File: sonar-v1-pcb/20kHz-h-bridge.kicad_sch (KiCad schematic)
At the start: 1 part, among them U34 DRV8876PWPR

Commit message: Do some power work
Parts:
- added C6: 22nF, GS_Capacitors:C_0603_1608Metric, symbol GS_Capacitor_0603:C_0603_22nF
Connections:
- net at U34.13 (CPH): now also C6.1
- net at U34.14 (CPL): now also C6.2
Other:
- moved on the sheet: U34
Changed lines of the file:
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@@
 		(comment 1 "George Sleen")
+	)
+	(wire
+		(pts
+			(xy 180.34 86.36) (xy 167.64 86.36)
+		)
+		(stroke
+			(width 0)
+			(type default)
+		)
+	)
+	(wire
+		(pts
+			(xy 180.34 78.74) (xy 167.64 78.74)
+		)
+		(stroke
+			(width 0)
+			(type default)
+		)
 	)
 	(symbol
 		(lib_id "GS_H_Bridges:DRV8876PWPR")
-		(at 148.59 104.14 0)
+		(at 147.32 102.87 0)
 		(unit 1)
 		(body_style 1)
@@
 		(fields_autoplaced yes)
 		(property "Reference" "U34"
-			(at 148.59 69.85 0)
+			(at 147.32 68.58 0)
 			(show_name no)
 			(do_not_autoplace no)
@@
 		)
 		(property "Value" "DRV8876PWPR"
-			(at 148.59 72.39 0)
+			(at 147.32 71.12 0)
 			(show_name no)
 			(do_not_autoplace no)
@@
 		)
 		(property "Footprint" "GS_SO:HTSSOP-16-1EP_4.4x5mm_P0.65mm_EP3.4x5mm_Mask2.46x2.31mm"
-			(at 148.59 53.34 0)
+			(at 147.32 52.07 0)
 			(hide yes)
 			(show_name no)
@@
 		)
 		(property "Datasheet" "https://lcsc.com/product-detail/Motor-Drivers_Texas-Instruments-Texas-Instruments-DRV8876PWPR_C575551.html"
-			(at 148.59 43.18 0)
+			(at 147.32 41.91 0)
 			(hide yes)
 			(show_name no)
@@
 		)
 		(property "Description" "H-Bridge wih Integrated Current Sense and Regulation, 4.5V - 37V Input Voltage Range, 6A Max Current"
-			(at 148.59 45.72 0)
+			(at 147.32 44.45 0)
 			(hide yes)
 			(show_name no)
@@
 		)
 		(property "Manufacturer" "TI"
-			(at 148.59 40.64 0)
+			(at 147.32 39.37 0)
 			(hide yes)
 			(show_name no)
@@
 		)
 		(property "MPN" "DRV8876PWPR"
-			(at 148.59 50.8 0)
+			(at 147.32 49.53 0)
 			(hide yes)
 			(show_name no)
@@
 		)
 		(property "LCSC ID" "C575551"
-			(at 148.59 55.88 0)
+			(at 147.32 54.61 0)
 			(hide yes)
 			(show_name no)
@@
 		)
 		(property "Package" "HTSSOP-16_L5.0-W4.4-P0.65-LS6.4-BL-EP"
-			(at 148.59 48.26 0)
+			(at 147.32 46.99 0)
 			(hide yes)
 			(show_name no)
@@
 					(unit 1)
 				)
+			)
+		)
+	)
+	(symbol
+		(lib_id "GS_Capacitor_0603:C_0603_22nF")
+		(at 180.34 82.55 0)
+		(unit 1)
+		(body_style 1)
+		(exclude_from_sim no)
+		(in_bom yes)
+		(on_board yes)
+		(in_pos_files yes)
+		(dnp no)
+		(fields_autoplaced yes)
+		(property "Reference" "C6"
+			(at 184.15 81.2799 0)
+			(show_name no)
+			(do_not_autoplace no)
+			(effects
+				(font
+					(size 1.27 1.27)
+				)
+				(justify left)
+			)
+		)
+		(property "Value" "22nF"
+			(at 184.15 83.8199 0)
+			(show_name no)
+			(do_not_autoplace no)
+			(effects
+				(font
+					(size 1.27 1.27)
+				)
+				(justify left)
+			)
+		)
+		(property "Footprint" "GS_Capacitors:C_0603_1608Metric"
+			(at 180.34 60.198 0)
+			(hide yes)
+			(show_name no)
+			(do_not_autoplace no)
+			(effects
+				(font
+					(size 1.27 1.27)
+				)
+			)
+		)
+		(property "Datasheet" "https://datasheet.lcsc.com/datasheet/pdf/02336ea48ea44ca18c72517dd3cb7b47.pdf?productCode=C21122"
+			(at 180.34 68.834 0)
+			(hide yes)
+			(show_name no)
+			(do_not_autoplace no)
+			(effects
+				(font
+					(size 1.27 1.27)
+				)
+			)
+		)
+		(property "Description" "22nF 10% Unpolarized Capacitor, 50V Max Voltage, X7R"
+			(at 180.34 66.802 0)
+			(hide yes)
+			(show_name no)
+			(do_not_autoplace no)
+			(effects
+				(font
+					(size 1.27 1.27)
+				)
+			)
+		)
+		(property "Manufacturer" "Samsung Electro-Mechanics"
+			(at 180.34 63.5 0)
+			(hide yes)
+			(show_name no)
+			(do_not_autoplace no)
+			(effects
+				(font
+					(size 1.27 1.27)
+				)
+			)
+		)
+		(property "MPN" "CL10B223KB8NNNC"
+			(at 180.34 65.278 0)
+			(hide yes)
+			(show_name no)
+			(do_not_autoplace no)
+			(effects
+				(font
+					(size 1.27 1.27)
+				)
+			)
+		)
+		(property "LCSC ID" "C21122"
+			(at 180.34 70.612 0)
+			(hide yes)
+			(show_name no)
+			(do_not_autoplace no)
+			(effects
+				(font
+					(size 1.27 1.27)
+				)
+			)
+		)
+		(property "Package" "0603"
+			(at 180.34 61.976 0)
+			(hide yes)
+			(show_name no)
+			(do_not_autoplace no)
+			(effects
+				(font
+					(size 1.27 1.27)
+				)
+			)
+		)
+		(pin "2"
+		)
+		(pin "1"
+		)
+		(instances
+			(project "sonar"
+				(path "/f72ceae0-eee4-4385-b0e8-639846bcb5f2/c6a046af-5387-4c6b-a77e-149ae78eccdc"
+					(reference "C6")
+					(unit 1)
+				)

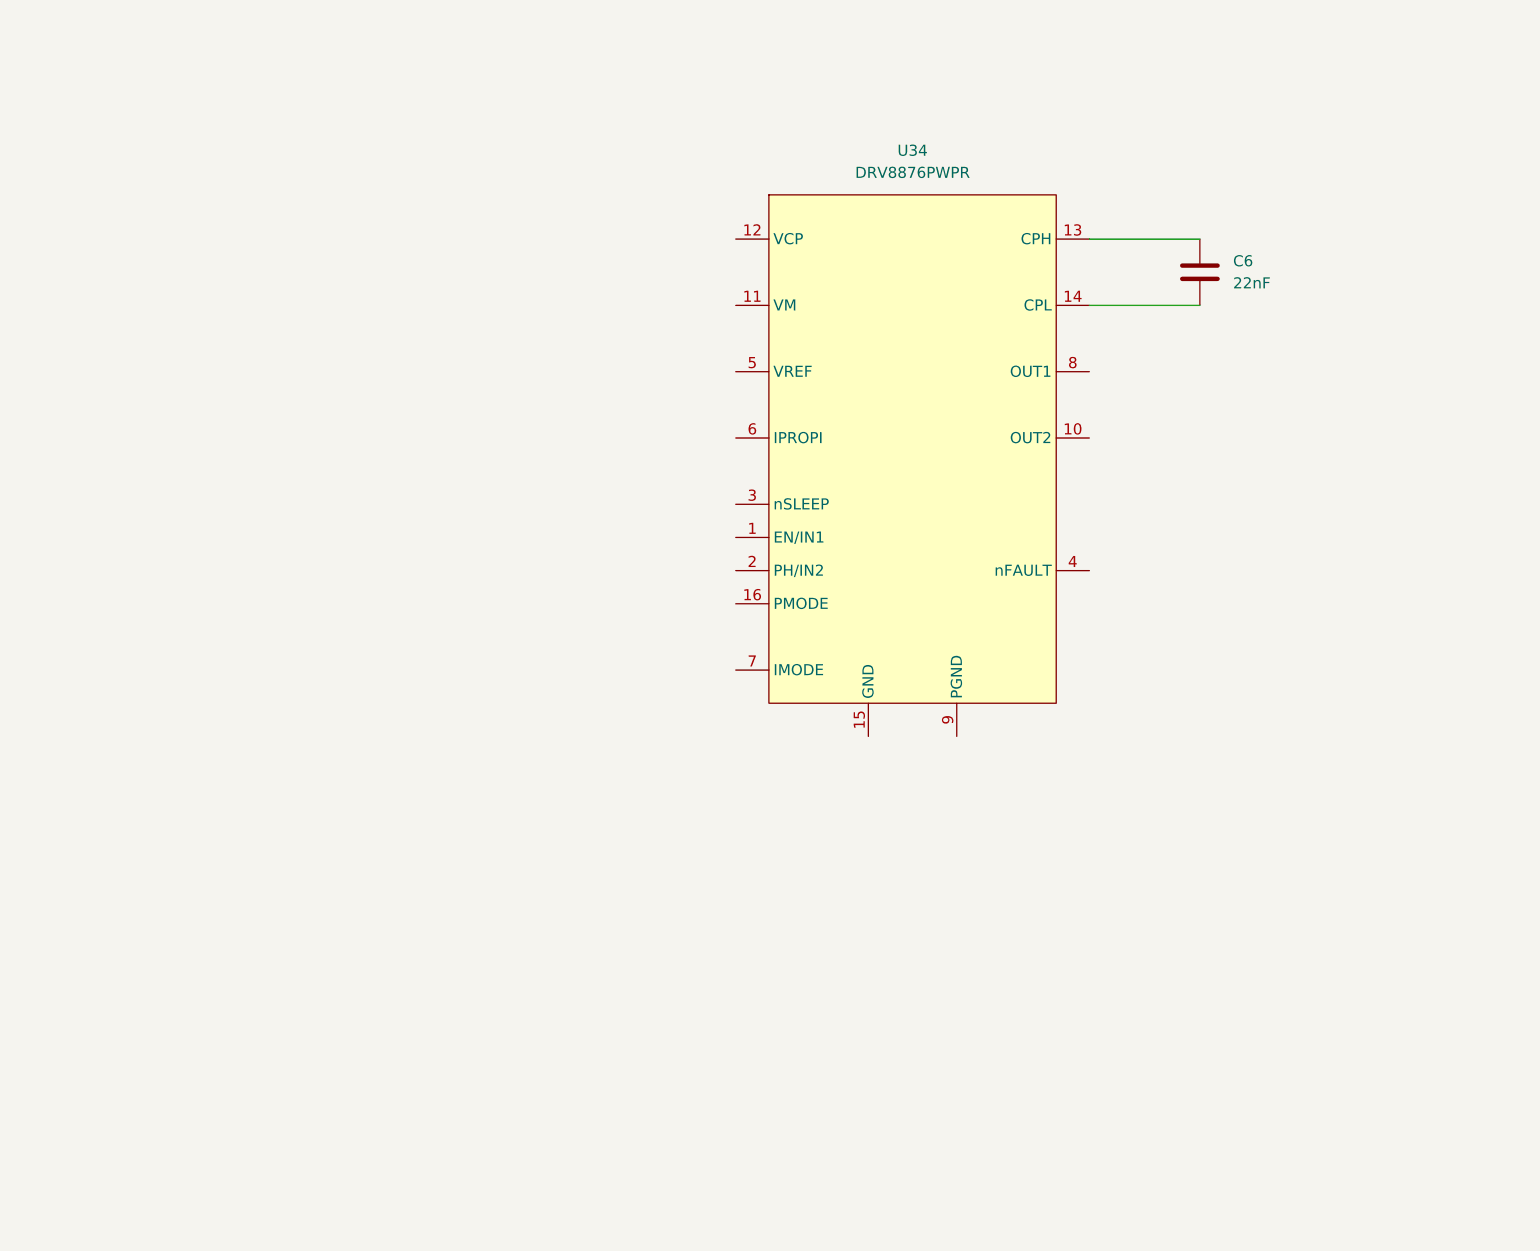
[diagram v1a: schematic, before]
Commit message: T-013: hook up DRV8876 h-bridge, off-board TX connector, C6 dup-ref fix
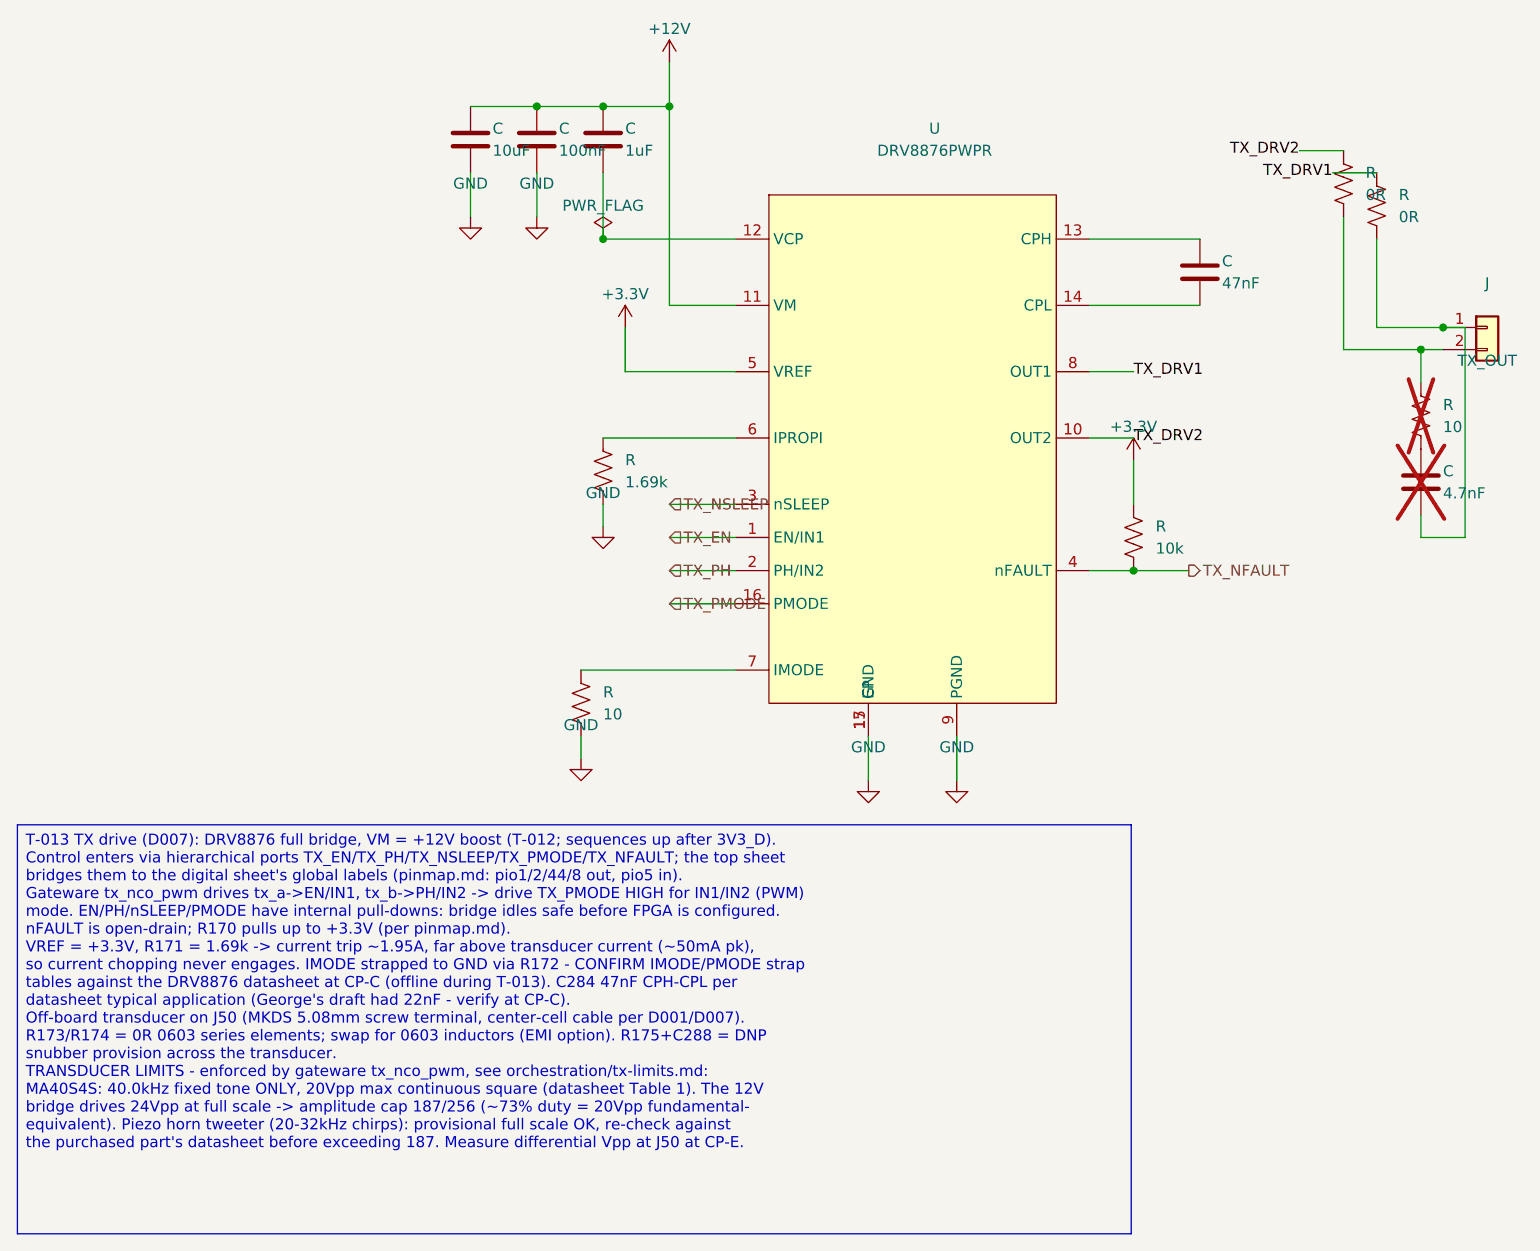
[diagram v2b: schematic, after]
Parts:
- removed C6: 22nF, GS_Capacitors:C_0603_1608Metric, symbol GS_Capacitor_0603:C_0603_22nF
- removed U34: DRV8876PWPR, GS_SO:HTSSOP-16-1EP_4.4x5mm_P0.65mm_EP3.4x5mm_Mask2.46x2.31mm, symbol GS_H_Bridges:DRV8876PWPR
- added C: 100nF, Sonar:C_0603_1608Metric, symbol sonar_lib:C_0603_100nF
- added C: 1uF, Sonar:C_0603_1608Metric, symbol sonar_lib:C_0603_1uF
- added C: 4.7nF, Sonar:C_0603_1608Metric, symbol sonar_lib:C_0603_4.7nF
- added C: 47nF, Sonar:C_0603_1608Metric, symbol sonar_lib:C_0603_47nF
- added C: 10uF, Sonar:C_0603_1608Metric, symbol sonar_lib:C_0603_10uF
- added J: TX_OUT, TerminalBlock_Phoenix:TerminalBlock_Phoenix_MKDS-1,5-2-5.08_1x02_P5.08mm_Horizontal, symbol Connector_Generic:Conn_01x02
- added R (x2): 10, Sonar:R_0603_1608Metric, symbol sonar_lib:R_0603_10
- added R (x2): 0R, Sonar:R_0603_1608Metric, symbol sonar_lib:R_0603_0R
- added R: 1.69k, Sonar:R_0603_1608Metric, symbol sonar_lib:R_0603_1.69k
- added R: 10k, Sonar:R_0603_1608Metric, symbol sonar_lib:R_0603_10k
- added U: DRV8876PWPR, Package_SO:HTSSOP-16-1EP_4.4x5mm_P0.65mm_EP3.4x5mm_Mask2.46x2.31mm, symbol sonar_lib:DRV8876PWPR
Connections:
- new net: J.2 (Pin_2), R.1, R.2
- new net: C.1, R.2
- new net: R.1, U.7 (IMODE)
- new net: C.2, U.12 (VCP)
- new net: C.2, J.1 (Pin_1), R.2
- new net: C.1, U.13 (CPH)
- new net: C.2, U.14 (CPL)
- new net: R.1, U.6 (IPROPI)
- new net +12V: C.1, C.1, C.1, U.11 (VM)
- new net +3.3V: R.1, U.5 (VREF)
- new net GND: C.2, C.2, R.2, R.2, U.15 (GND), U.17 (EP), U.9 (PGND)
- new net TX_DRV1: R.1, U.8 (OUT1)
- new net TX_DRV2: R.1, U.10 (OUT2)
- new net TX_EN: U.1 (EN/IN1)
- new net TX_NFAULT: R.2, U.4 (nFAULT)
- new net TX_NSLEEP: U.3 (nSLEEP)
- new net TX_PH: U.2 (PH/IN2)
- new net TX_PMODE: U.16 (PMODE)
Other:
- title: 20kHz H-Bridge -> TX Drive - DRV8876 H-Bridge
